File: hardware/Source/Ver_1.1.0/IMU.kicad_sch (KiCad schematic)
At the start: 0 parts

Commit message: update pcb v1.1.0
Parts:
- added C33: 10uF, automative_hexapod:Ceramic_Cap_0805, symbol automative_hexapod:Ceramic_Cap_0805_10uF_16V
- added C34: 100nF, automative_hexapod:Ceramic_Cap_0805, symbol automative_hexapod:Ceramic_Cap_0805_100nF_50V
- added J4: MPU6050, automative_hexapod:MPU6050, symbol automative_hexapod:MPU6050
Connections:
- new net +5V: C33.2, C34.2, J4.1 (Pin_1)
- new net GND: C33.1, C34.1, J4.2 (Pin_2)
- new net MPU6050_I2C_SCL: J4.3 (Pin_3)
- new net MPU6050_I2C_SDA: J4.4 (Pin_4)
- no-connect marks 0 -> 4
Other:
- title: (none) -> IMU

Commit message: update pcb and schematic
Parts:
- renumbered C33 to C27, C34 to C28
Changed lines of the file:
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@@
 		(on_board yes)
 		(dnp no)
-		(property "Reference" "#PWR085"
+		(property "Reference" "#PWR083"
 			(at 143.51 90.17 0)
 			(effects
@@
 			(project "Automative_Hexapod"
 				(path "/c07b6013-2147-4cef-a16e-342deb9ccbf5/6f119c3f-94db-4ed9-9af0-8eee89c2f72e"
-					(reference "#PWR085")
+					(reference "#PWR083")
 					(unit 1)
 				)
@@
 		(dnp no)
 		(fields_autoplaced yes)
-		(property "Reference" "#PWR086"
+		(property "Reference" "#PWR084"
 			(at 149.86 90.17 0)
 			(effects
@@
 			(project "Automative_Hexapod"
 				(path "/c07b6013-2147-4cef-a16e-342deb9ccbf5/6f119c3f-94db-4ed9-9af0-8eee89c2f72e"
-					(reference "#PWR086")
+					(reference "#PWR084")
 					(unit 1)
 				)
@@
 		(dnp no)
 		(fields_autoplaced yes)
-		(property "Reference" "#PWR088"
+		(property "Reference" "#PWR086"
 			(at 184.15 110.49 0)
 			(effects
@@
 			(project "Automative_Hexapod"
 				(path "/c07b6013-2147-4cef-a16e-342deb9ccbf5/6f119c3f-94db-4ed9-9af0-8eee89c2f72e"
-					(reference "#PWR088")
+					(reference "#PWR086")
 					(unit 1)
 				)
@@
 		(on_board yes)
 		(dnp no)
-		(property "Reference" "#PWR087"
+		(property "Reference" "#PWR085"
 			(at 184.15 90.17 0)
 			(effects
@@
 			(project "Automative_Hexapod"
 				(path "/c07b6013-2147-4cef-a16e-342deb9ccbf5/6f119c3f-94db-4ed9-9af0-8eee89c2f72e"
-					(reference "#PWR087")
+					(reference "#PWR085")
 					(unit 1)
 				)
@@
 		(on_board yes)
 		(dnp no)
-		(property "Reference" "C34"
+		(property "Reference" "C28"
 			(at 195.58 95.25 90)
 			(effects
@@
 			(project ""
 				(path "/c07b6013-2147-4cef-a16e-342deb9ccbf5/6f119c3f-94db-4ed9-9af0-8eee89c2f72e"
-					(reference "C34")
+					(reference "C28")
 					(unit 1)
 				)
@@
 		(on_board yes)
 		(dnp no)
-		(property "Reference" "C33"
+		(property "Reference" "C27"
 			(at 176.53 95.25 90)
 			(effects
@@
 			(project ""
 				(path "/c07b6013-2147-4cef-a16e-342deb9ccbf5/6f119c3f-94db-4ed9-9af0-8eee89c2f72e"
-					(reference "C33")
-					(unit 1)
-				)
+					(reference "C27")
+					(unit 1)
+				)

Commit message: Update PCB Ver_1.1.0
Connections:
- net MPU6050_I2C_SCL renamed BBAI_I2C_SCL
- net MPU6050_I2C_SDA renamed BBAI_I2C_SDA
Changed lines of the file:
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@@
 		)
 	)
-	(global_label "MPU6050_I2C_SDA"
+	(global_label "BBAI_I2C_SDA"
 		(shape bidirectional)
 		(at 144.78 95.25 0)
@@
 		)
 		(property "Intersheetrefs" "${INTERSHEET_REFS}"
-			(at 166.354 95.25 0)
+			(at 161.6975 95.25 0)
 			(effects
 				(font
@@
 		)
 	)
-	(global_label "MPU6050_I2C_SCL"
+	(global_label "BBAI_I2C_SCL"
 		(shape input)
 		(at 144.78 92.71 0)
@@
 		)
 		(property "Intersheetrefs" "${INTERSHEET_REFS}"
-			(at 165.1822 92.71 0)
+			(at 160.5257 92.71 0)
 			(effects
 				(font

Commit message: Update PCB_Ver1.1.0
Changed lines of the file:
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@@
 		(on_board yes)
 		(dnp no)
-		(property "Reference" "#PWR083"
+		(property "Reference" "#PWR084"
 			(at 143.51 90.17 0)
 			(effects
@@
 			(project "Automative_Hexapod"
 				(path "/c07b6013-2147-4cef-a16e-342deb9ccbf5/6f119c3f-94db-4ed9-9af0-8eee89c2f72e"
-					(reference "#PWR083")
+					(reference "#PWR084")
 					(unit 1)
 				)
@@
 		(dnp no)
 		(fields_autoplaced yes)
-		(property "Reference" "#PWR084"
+		(property "Reference" "#PWR085"
 			(at 149.86 90.17 0)
 			(effects
@@
 			(project "Automative_Hexapod"
 				(path "/c07b6013-2147-4cef-a16e-342deb9ccbf5/6f119c3f-94db-4ed9-9af0-8eee89c2f72e"
-					(reference "#PWR084")
+					(reference "#PWR085")
 					(unit 1)
 				)
@@
 		(dnp no)
 		(fields_autoplaced yes)
-		(property "Reference" "#PWR086"
+		(property "Reference" "#PWR087"
 			(at 184.15 110.49 0)
 			(effects
@@
 			(project "Automative_Hexapod"
 				(path "/c07b6013-2147-4cef-a16e-342deb9ccbf5/6f119c3f-94db-4ed9-9af0-8eee89c2f72e"
-					(reference "#PWR086")
+					(reference "#PWR087")
 					(unit 1)
 				)
@@
 		(on_board yes)
 		(dnp no)
-		(property "Reference" "#PWR085"
+		(property "Reference" "#PWR086"
 			(at 184.15 90.17 0)
 			(effects
@@
 			(project "Automative_Hexapod"
 				(path "/c07b6013-2147-4cef-a16e-342deb9ccbf5/6f119c3f-94db-4ed9-9af0-8eee89c2f72e"
-					(reference "#PWR085")
+					(reference "#PWR086")
 					(unit 1)
 				)
@@
 		)
 		(property "Value 2" "50V"
-			(at 207.01 93.726 90)
+			(at 208.534 96.012 0)
 			(effects
 				(font
@@
 					(color 0 132 132 1)
 				)
-				(justify right)
 			)
 		)
 		(property "Value 3" "0805"
-			(at 207.01 96.266 90)
+			(at 210.312 95.25 0)
 			(effects
 				(font
@@
 					(color 0 132 132 1)
 				)
-				(justify right)
 			)
 		)
 		(property "Value 4" "10%"
-			(at 207.01 98.806 90)
+			(at 212.09 95.758 0)
 			(effects
 				(font
@@
 					(color 0 132 132 1)
 				)
-				(justify right)
 			)
 		)
@@
 		)
 		(property "Value 2" "16V"
-			(at 187.96 93.98 90)
+			(at 188.976 94.996 0)
 			(effects
 				(font
@@
 					(color 0 132 132 1)
 				)
-				(justify right)
 			)
 		)
 		(property "Value 3" "0805"
-			(at 187.96 96.52 90)
+			(at 190.754 94.234 0)
 			(effects
 				(font
@@
 					(color 0 132 132 1)
 				)
-				(justify right)
 			)
 		)
 		(property "Value 4" "10%"
-			(at 187.96 99.06 90)
+			(at 192.532 94.742 0)
 			(effects
 				(font
@@
 					(color 0 132 132 1)
 				)
-				(justify right)
-			)
-		)
+			)
+		)

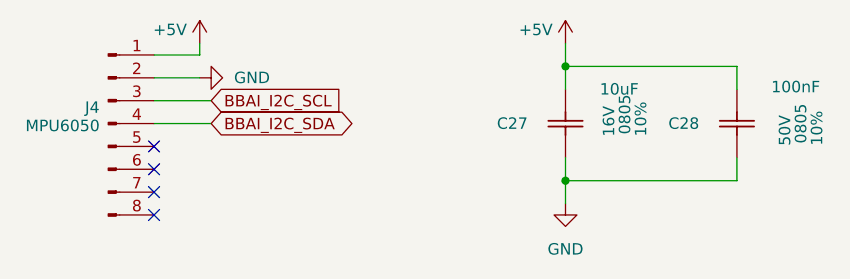
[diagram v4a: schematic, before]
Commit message: Generate PDF Schematic Ver1.1.0 and add README.md
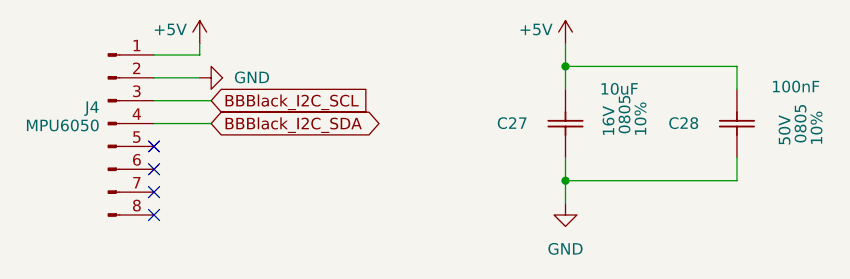
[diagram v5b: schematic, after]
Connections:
- net BBAI_I2C_SCL renamed BBBlack_I2C_SCL
- net BBAI_I2C_SDA renamed BBBlack_I2C_SDA
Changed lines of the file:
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@@
 		)
 	)
-	(global_label "BBAI_I2C_SDA"
+	(global_label "BBBlack_I2C_SDA"
 		(shape bidirectional)
 		(at 144.78 95.25 0)
@@
 		)
 	)
-	(global_label "BBAI_I2C_SCL"
+	(global_label "BBBlack_I2C_SCL"
 		(shape input)
 		(at 144.78 92.71 0)
